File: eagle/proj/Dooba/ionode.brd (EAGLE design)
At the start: 27.4 x 27.4 mm, 25 parts, among them P1 PIN_2, P2 PIN_2, P3 PIN_2, P4 PIN_2, U1 ATMEGA328PB32-VQFN, U2 LP3985SOT23-5, U3 MIC550XSOT23, U4 WRL-13678WRL-13678-QUIET, U5 SN74LVC1G125SOT23-5, U6 SN74LVC1G125SOT23-5, X1 20MHz

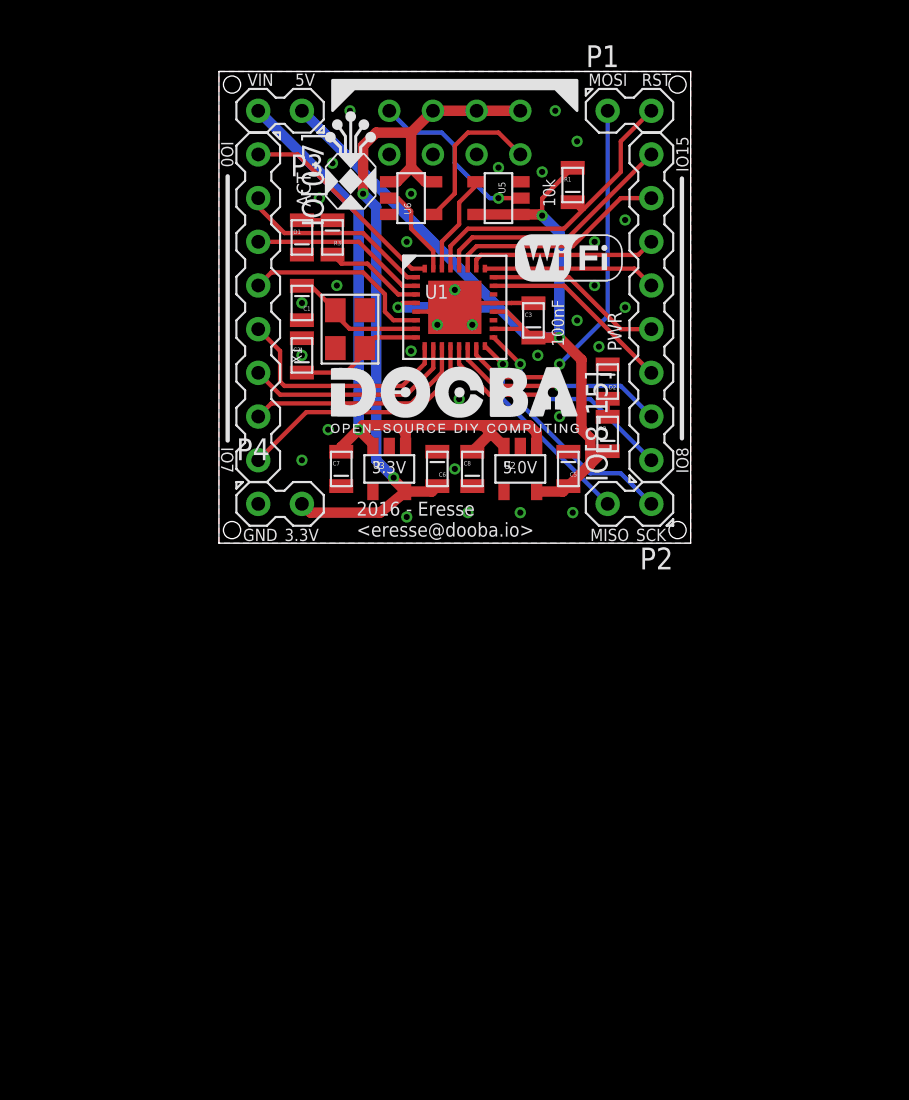
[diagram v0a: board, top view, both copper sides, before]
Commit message: Redesigned ioNode using ATMEGA1284P, replaced esp8266 with ft232rq usb/serial
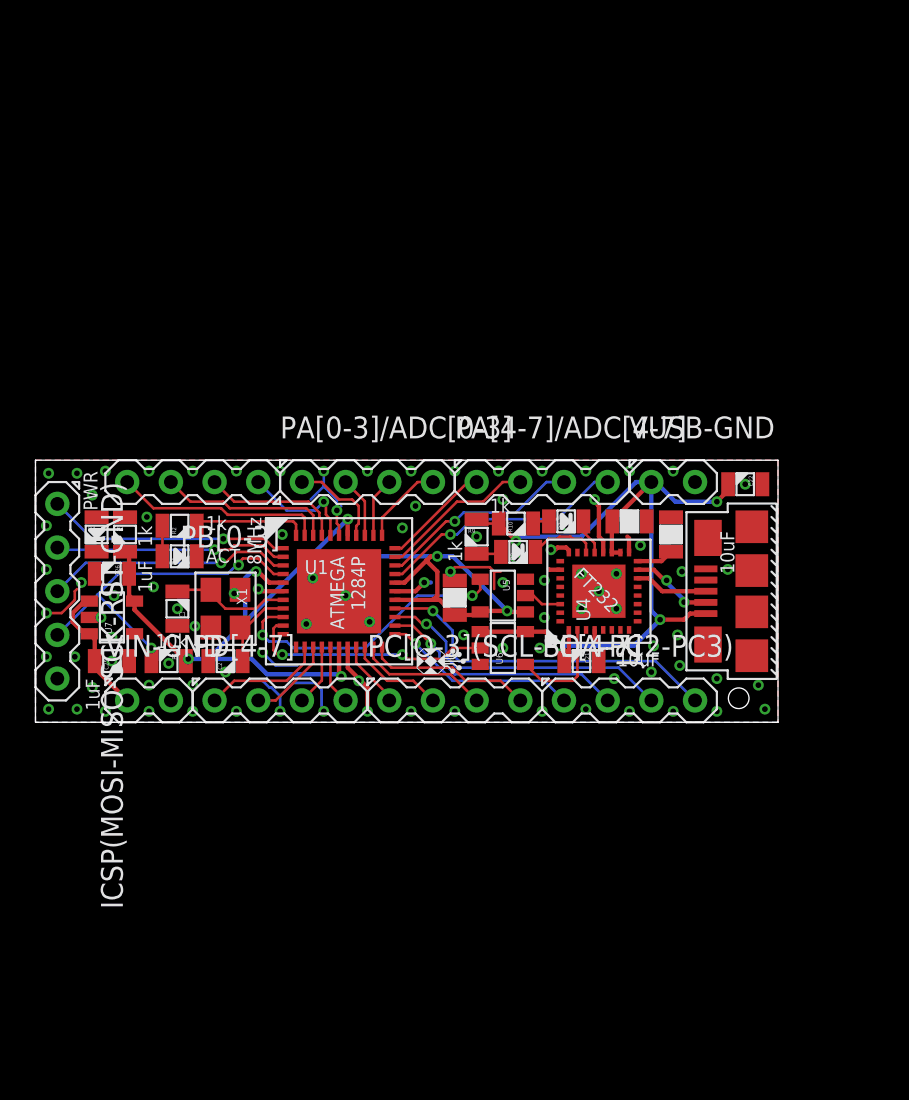
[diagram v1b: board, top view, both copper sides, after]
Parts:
- removed C5, C6, C7, C8: 1uF, dooba:0805
- removed IO[0-7], IO[8-15]: PIN_8, dooba:PIN_8
- removed P1, P2, P3, P4: PIN_2, dooba:PIN_2
- removed U2: LP3985SOT23-5, dooba:SOT23-5
- removed U3: MIC550XSOT23, dooba:SOT23-5
- added C21, C22: 10uF, dooba:0805
- added C23, C24: 100nF, dooba:0805
- added C25, C26: 1uF, dooba:0805
- added D3: TX, dooba:0805
- added D4: PWR, dooba:0805
- added ICSP(MOSI-MISO-SCK-RST-GND): PIN_5, dooba:PIN_5
- added J2: USB-BAMPHENOL-MICRO, dooba:AMPHENOL-USB-MICRO-B
- added PA[0-3]/ADC[0-3], PA[4-7]/ADC[4-7], PB[0-3], PC[4-7], PC[O-3](SCL-SDA-PC2-PC3), PD[4-7]: PIN_4, dooba:PIN_4
- added R10, R9: 1k, dooba:0805
- added U7: 3.3V, dooba:SOT23-5
- added VIN-GND, VUSB-GND: PIN_2, dooba:PIN_2
- D2: value PWR -> RX
- R2, R3: value 330R -> 1k
- U1: value ATMEGA328PB32-VQFN -> ATMEGA1284P-MU44-VQFN; device dooba:32-VQFN -> dooba:44-VQFN
- U4: value WRL-13678WRL-13678-QUIET -> FT232RQFN32; device dooba:WRL-13678-QUIET -> dooba:32-VQFN
- X1: value 20MHz -> 10MHz
- moved R1 36.3 mm to (31.6, 29.0), turned to 180 degrees
- moved U6 26.7 mm to (51.1, 29.7)
- moved R2 25.5 mm to (32.3, 36.8), turned to 0 degrees
- moved U5 23.1 mm to (51.1, 32.8)
- moved R3 21.1 mm to (29.1, 36.3), turned to 270 degrees
- moved D1 19.9 mm to (32.3, 35.1), turned to 0 degrees
- moved C1 19.2 mm to (32.1, 32.0)
- moved U4 18.5 mm to (56.6, 33.0), flipped to the top, turned to 90 degrees
- moved C2 18.3 mm to (34.9, 29.0), turned to 0 degrees
- moved U1 17.8 mm to (41.5, 33.0)
- moved X1 17.8 mm to (34.9, 32.0), turned to 270 degrees
- moved C3 16.8 mm to (48.3, 32.6), turned to 90 degrees
- moved D2 11.2 mm to (51.9, 35.3), turned to 0 degrees
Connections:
- removed net N$10: C6.1, P4.2, U3.5, U4.4, U4.6, U4.8, U6.1, U6.5
- removed net N$11: U4.2, U5.2
- removed net N$12: U1.P$30, U5.4
- removed net N$13: U1.P$31, U6.2
- removed net N$14: P1.1, U1.P$15
- removed net N$15: P2.2, U1.P$16
- removed net N$16: P2.1, U1.P$17
- removed net N$17: IO[0-7].2, U1.P$1
- removed net N$18: IO[0-7].3, U1.P$2
- removed net N$19: IO[0-7].4, U1.P$6
- removed net N$20: IO[0-7].5, U1.P$9
- removed net N$28: IO[8-15].5, U1.P$25
- removed net N$29: IO[8-15].6, U1.P$26
- removed net N$30: IO[8-15].7, U1.P$27
- removed net N$31: IO[8-15].8, U1.P$28
- removed net N$4: P1.2, R1.2, U1.P$29
- removed net N$7: D1.1, R3.2
- removed net N$8: C1.2, U1.P$7, X1.3
- removed net N$9: C2.2, U1.P$8, X1.1
- removed net VCC: C3.2, C5.1, P3.1, R1.1, R2.2, U1.P$18, U1.P$20, U1.P$4, U2.5, U5.1, U5.5
- new net !RESET: ICSP(MOSI-MISO-SCK-RST-GND).4, R1.2, U1.4
- new net 3.3V: C26.1, C3.1, R1.1, R3.2, U1.17, U1.27, U1.29, U1.38, U1.5, U5.1, U5.5, U7.5
- new net ATMEGA_RX: U1.9, U5.4
- new net ATMEGA_TX: U1.10, U6.2
- new net FT232R_RX: U4.P$2, U6.4
- new net FT232R_TX: U4.P$30, U5.2
- new net PA0/ADC0: PA[0-3]/ADC[0-3].1, U1.37
- new net PA1/ADC1: PA[0-3]/ADC[0-3].2, U1.36
- new net PA2/ADC2: PA[0-3]/ADC[0-3].3, U1.35
- new net PA3/ADC3: PA[0-3]/ADC[0-3].4, U1.34
- new net PA4/ADC4: PA[4-7]/ADC[4-7].1, U1.33
- new net PA5/ADC5: PA[4-7]/ADC[4-7].2, U1.32
- new net PA6/ADC6: PA[4-7]/ADC[4-7].3, U1.31
- new net PA7/ADC7: PA[4-7]/ADC[4-7].4, U1.30
- new net PB0: PB[0-3].1, U1.40
- new net PB1: PB[0-3].2, U1.41
- new net PB2: PB[0-3].3, U1.42
- new net PB3: PB[0-3].4, U1.43
- new net PB5/MOSI: ICSP(MOSI-MISO-SCK-RST-GND).1, U1.1
- new net PB6/MISO: ICSP(MOSI-MISO-SCK-RST-GND).2, U1.2
- new net PB7/SCK: ICSP(MOSI-MISO-SCK-RST-GND).3, U1.3
- new net PC0/SCL: PC[O-3](SCL-SDA-PC2-PC3).1, U1.19
- new net PC1/SDA: PC[O-3](SCL-SDA-PC2-PC3).2, U1.20
- new net PC2: PC[O-3](SCL-SDA-PC2-PC3).3, U1.21
- new net PC3: PC[O-3](SCL-SDA-PC2-PC3).4, U1.22
- new net PC4: PC[4-7].1, U1.23
- new net PC5: PC[4-7].2, U1.24
- new net PC6: PC[4-7].3, U1.25
- new net PC7: PC[4-7].4, U1.26
- new net PD2/RXD1: U1.11
- new net PD3/TXD1: U1.12
- new net PD4: PD[4-7].1, U1.13
- new net PD5: PD[4-7].2, U1.14
- new net PD6: PD[4-7].3, U1.15
- new net PD7: PD[4-7].4, U1.16
- new net VIN: C25.1, U7.1, U7.3, VIN-GND.1
- new net VUSB: C21.2, C22.2, C23.2, J2.1, R10.1, R9.1, U4.P$1, U4.P$18, U4.P$19, U6.1, U6.5, VUSB-GND.1
- net GND: now also C21.1, C22.1, C23.1, C24.1, C25.2, C26.2, C3.2, D4.2, ICSP(MOSI-MISO-SCK-RST-GND).5, J2.5, J2.P$10, J2.P$11, J2.P$6, J2.P$7, J2.P$8, J2.P$9, U1.18, U1.28, U1.39, U1.6, U1.TH, U4.P$17, U4.P$20, U4.P$24, U4.P$26, U4.P$33, U4.P$4, U7.2, VIN-GND.2, VUSB-GND.2; no longer C3.1, C5.2, C6.2, C7.2, C8.2, D2.2, P4.1, U1.P$21, U1.P$33, U1.P$5, U2.2, U3.2, U4.1
- net N$1: now also C2.2, U1.8, X1.3; no longer C7.1, C8.1, P3.2, U2.1, U2.3, U3.1, U3.3
- net N$2: now also C1.2, U1.7, X1.1; no longer IO[0-7].1, U1.P$32
- net N$21: now also C24.2, U4.P$16; no longer IO[0-7].6, U1.P$10
- net N$22: now also D2.2, U4.P$22; no longer IO[0-7].7, U1.P$11
- net N$23: now also D3.2, U4.P$21; no longer IO[0-7].8, U1.P$12
- net N$24: now also D2.1, R9.2; no longer IO[8-15].1, U1.P$13
- net N$25: now also D3.1, R10.2; no longer IO[8-15].2, U1.P$14
- net N$26: now also J2.2, U4.P$15; no longer IO[8-15].3, U1.P$23
- net N$27: now also J2.3, U4.P$14; no longer IO[8-15].4, U1.P$24
- net N$3: now also D4.1, R3.1; no longer D2.1, R2.1
- net N$5: now also D1.1, R2.1; no longer U4.7, U6.4
- net N$6: now also R2.2, U1.44; no longer R3.1, U1.P$3
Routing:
- net 3.3V: track 0.00 -> 63.3 mm, vias 0 -> 6
- net VCC: track 61.8 -> 0.00 mm, vias 3 -> 0
- net VUSB: track 0.00 -> 48.6 mm, vias 0 -> 4
- net N$10: track 45.1 -> 0.00 mm, vias 2 -> 0
- net N$1: track 40.1 -> 4.98 mm, vias 1 -> 0
- net GND: track 8.02 -> 36.0 mm, vias 32 -> 97
- net N$14: track 22.1 -> 0.00 mm, vias 1 -> 0
- net !RESET: track 0.00 -> 20.6 mm, vias 0 -> 2
- net PC7: track 0.00 -> 20.5 mm, vias 0 -> 1
- net N$4: track 18.1 -> 0.00 mm
- net PC6: track 0.00 -> 17.4 mm, vias 0 -> 1
- net ATMEGA_RX: track 0.00 -> 17.1 mm, vias 0 -> 2
- net PA7/ADC7: track 0.00 -> 14.6 mm, vias 0 -> 1
- net N$31: track 14.5 -> 0.00 mm
- net N$16: track 14.5 -> 0.00 mm, vias 1 -> 0
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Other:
- board size 27.4 x 27.4 mm -> 43.2 x 15.2 mm
- board text added: "10uF"
- board text added: "1k"
- board text added: "1uF"
- board text added: "8MHz"
- board text added: "ATMEGA 1284P"
- board text added: "FT232"
- board text removed: "100nF"
- board text removed: "2016 - Eresse <eresse@dooba.io>"
- board text removed: "3.3V"
- board text removed: "5.0V"
- board text removed: "5V"
- board text removed: "GND"
- board text removed: "IO0"
- board text removed: "IO15"
- board text removed: "IO7"
- board text removed: "IO8"
- board text removed: "MISO"
- board text removed: "MOSI"
- board text removed: "RST"
- board text removed: "SCK"
- board text removed: "VIN"
